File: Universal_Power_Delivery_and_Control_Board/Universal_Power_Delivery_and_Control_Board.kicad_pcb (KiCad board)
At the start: 2 copper layers, 49 parts, among them Q1 AO4407A, Q2 AO4407A, Q3 AO3401A, U1 CH224Q_C46061833, U2 TPS54202DDC, U3 USBLC6-2SC6, U4 USBLC6-2SC6, U5 ESD2CAN24-ES, U6 S2B-ZR (LF)(SN), U7 TPS259470LRPWR

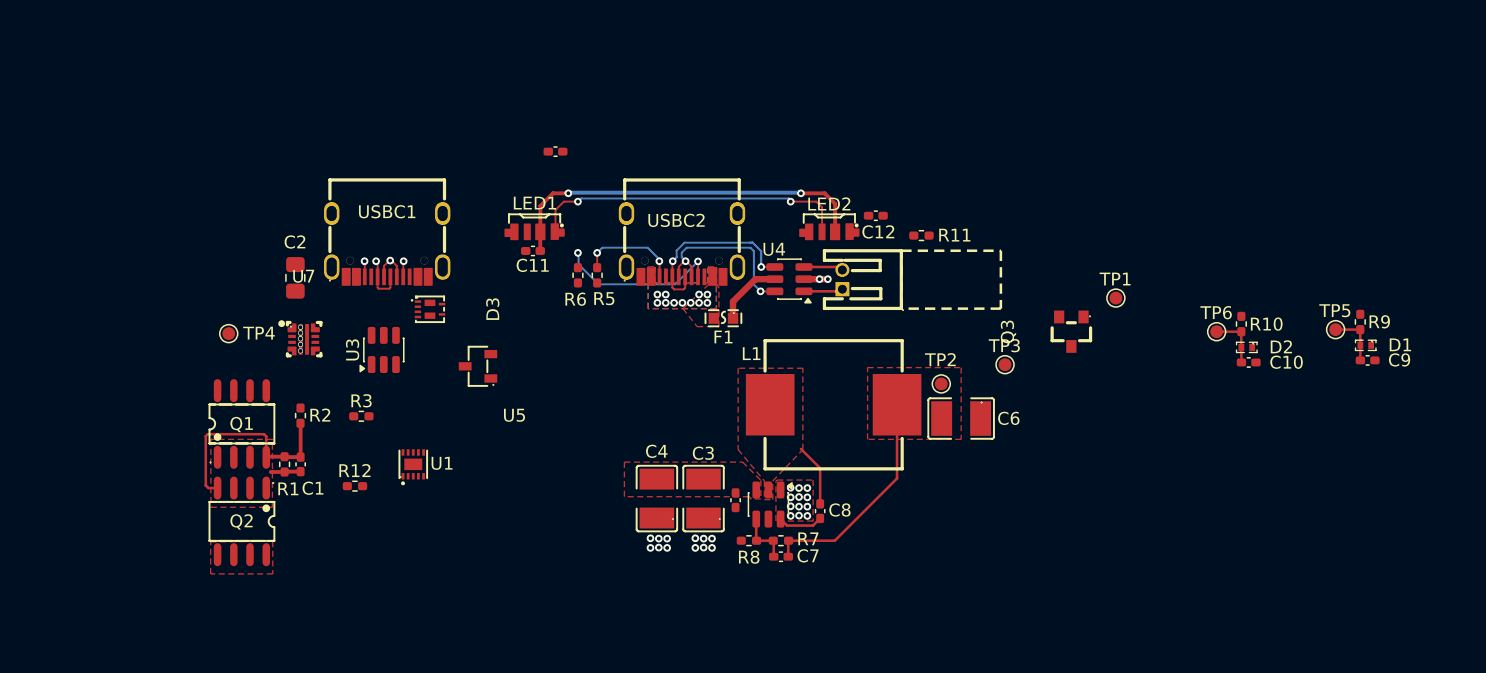
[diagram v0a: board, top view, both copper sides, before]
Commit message: Continued with routing on the UPDC and minor changes on the matrix board.
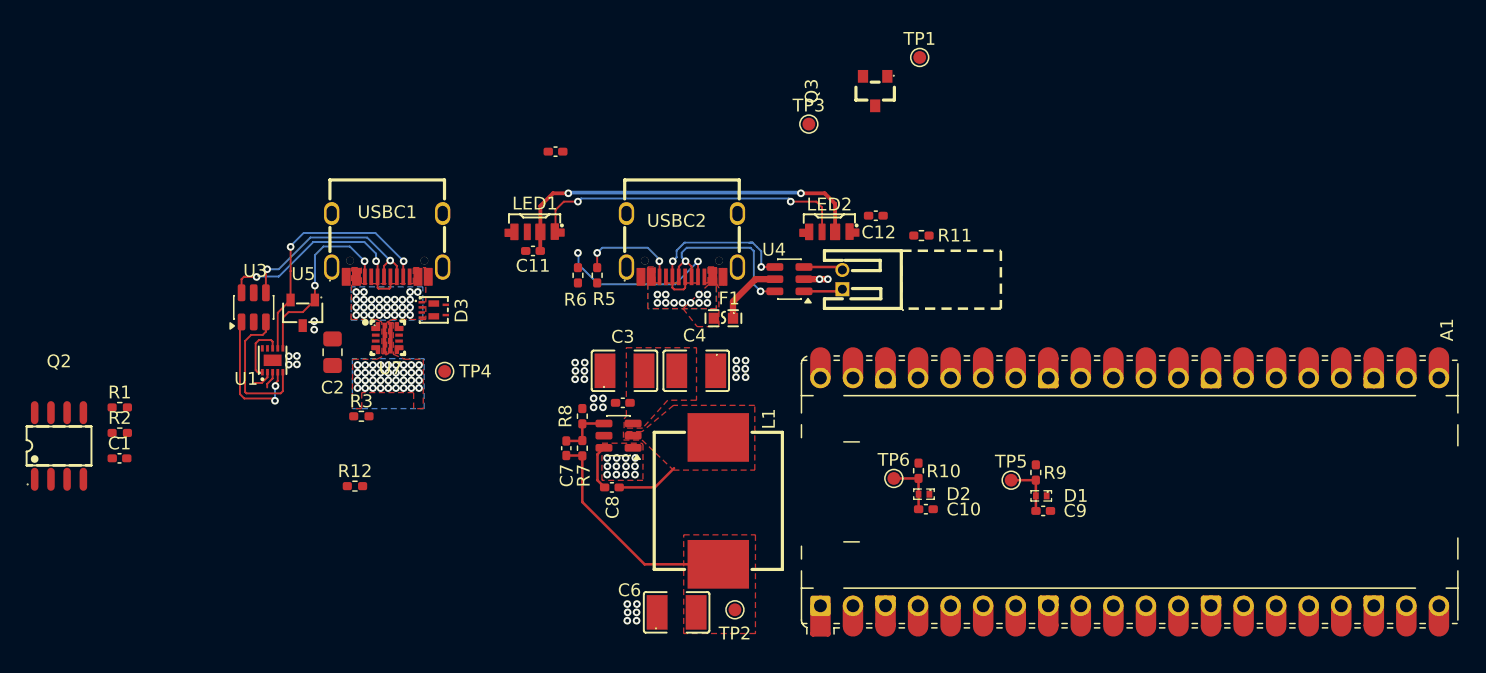
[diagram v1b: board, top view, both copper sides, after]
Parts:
- removed Q1: AO4407A, lcsc_footprints:C16072_SOIC-8_L4_9-W3_9-P1_27-LS6_0-BL
- added A1: RaspberryPi_Pico, Module:RaspberryPi_Pico_Common_Unspecified, F.Cu at (174.1, 61.8)
- moved C9 27.9 mm to (167.3, 63.3)
- moved D1 27.9 mm to (167.2, 62.1)
- moved R9 27.9 mm to (166.7, 60.3)
- moved TP5 27.9 mm to (164.8, 60.9)
- moved D2 27.7 mm to (158.0, 62.0)
- moved TP6 27.7 mm to (155.7, 60.8)
- moved C10 27.7 mm to (158.2, 63.1)
- moved R10 27.7 mm to (157.6, 60.1)
- moved C6 26.9 mm to (138.7, 71.2), turned to 0 degrees
- moved Q3 24.2 mm to (154.2, 30.5)
- moved TP1 24.2 mm to (157.7, 27.9)
- moved TP3 24.2 mm to (149.0, 33.1)
- moved TP2 23.9 mm to (143.2, 71.0), turned to 0 degrees
- moved C7 18.8 mm to (130.1, 58.4), turned to 90 degrees
- moved TP4 17.1 mm to (120.6, 52.4)
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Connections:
- net Net-(USBC1-DN1) renamed /PD_Section/USB1sub_D-
- net Net-(USBC1-DP1) renamed /PD_Section/USB1sub_D+
- U7 pad 6: Net-(U7-OUT) -> unconnected-(U7-OUT-Pad6)
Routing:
- net Net-(U1-CC1): track 1.23 -> 19.8 mm, vias 1 -> 2
- net Net-(Q2-G): track 16.7 -> 0.00 mm
- net /PD_Section/USB1sub_D+: track 4.03 -> 17.8 mm, vias 1 -> 2
- net Net-(U1-CC2): track 1.22 -> 14.8 mm, vias 1 -> 2
- net /PD_Section/USB1sub_D-: track 3.05 -> 16.3 mm, vias 1 -> 2
- net /PD_Section/USB1_D-: track 0.00 -> 11.2 mm
- net /PD_Section/USB1_D+: track 0.00 -> 11.0 mm, vias 0 -> 2
- net /PD_Section/PD_VBUS: track 0.00 -> 4.69 mm, vias 5 -> 28
- net Net-(C1-Pad1): track 2.32 -> 0.00 mm
- net /PD_Section/SCL: track 0.00 -> 1.60 mm
- net /PD_Section/SDA: track 0.00 -> 1.37 mm
- net unconnected-(U7-OUT-Pad6): vias 0 -> 36
- net GND: vias 26 -> 42
- added copper zone on B.Cu, net /PD_Section/PD_VBUS
- added copper zone on F.Cu, net Net-(U2-VIN)
- added copper zone on B.Cu, net unconnected-(U7-OUT-Pad6)
- added copper zone on F.Cu, net unconnected-(U7-OUT-Pad6)
- removed copper zone on F.Cu, net +12V_PD
- removed copper zone on F.Cu, net Net-(C1-Pad1)
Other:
- board text added: "Inductor Keep Out"
